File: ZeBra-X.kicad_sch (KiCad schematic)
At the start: 0 parts

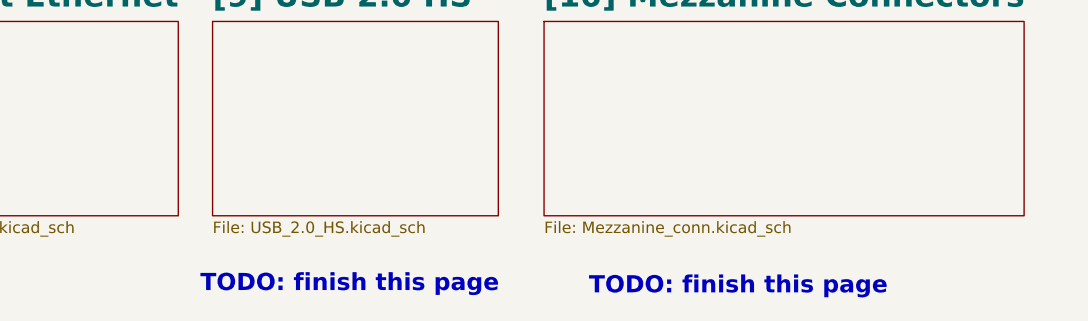
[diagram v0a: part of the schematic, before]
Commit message: Finished first pass of schematic, needs netclass assignments and double check
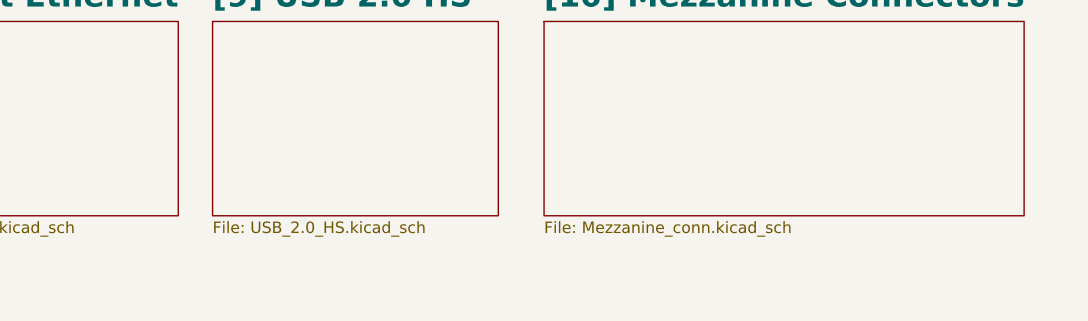
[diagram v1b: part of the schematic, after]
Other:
- note removed: "TODO: finish this page"
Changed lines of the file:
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@@
-		)
-	)
-	(text "TODO: finish this page"
-		(exclude_from_sim no)
-		(at 247.65 118.364 0)
-		(effects
-			(font
-				(size 1.905 1.905)
-				(thickness 0.381)
-				(bold yes)
-			)
-		)
-	)
-	(text "TODO: finish this page"
-		(exclude_from_sim no)
-		(at 204.47 118.11 0)
-		(effects
-			(font
-				(size 1.905 1.905)
-				(thickness 0.381)
-				(bold yes)
-			)
 		)
 	)
